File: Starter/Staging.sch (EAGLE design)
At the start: 2 parts

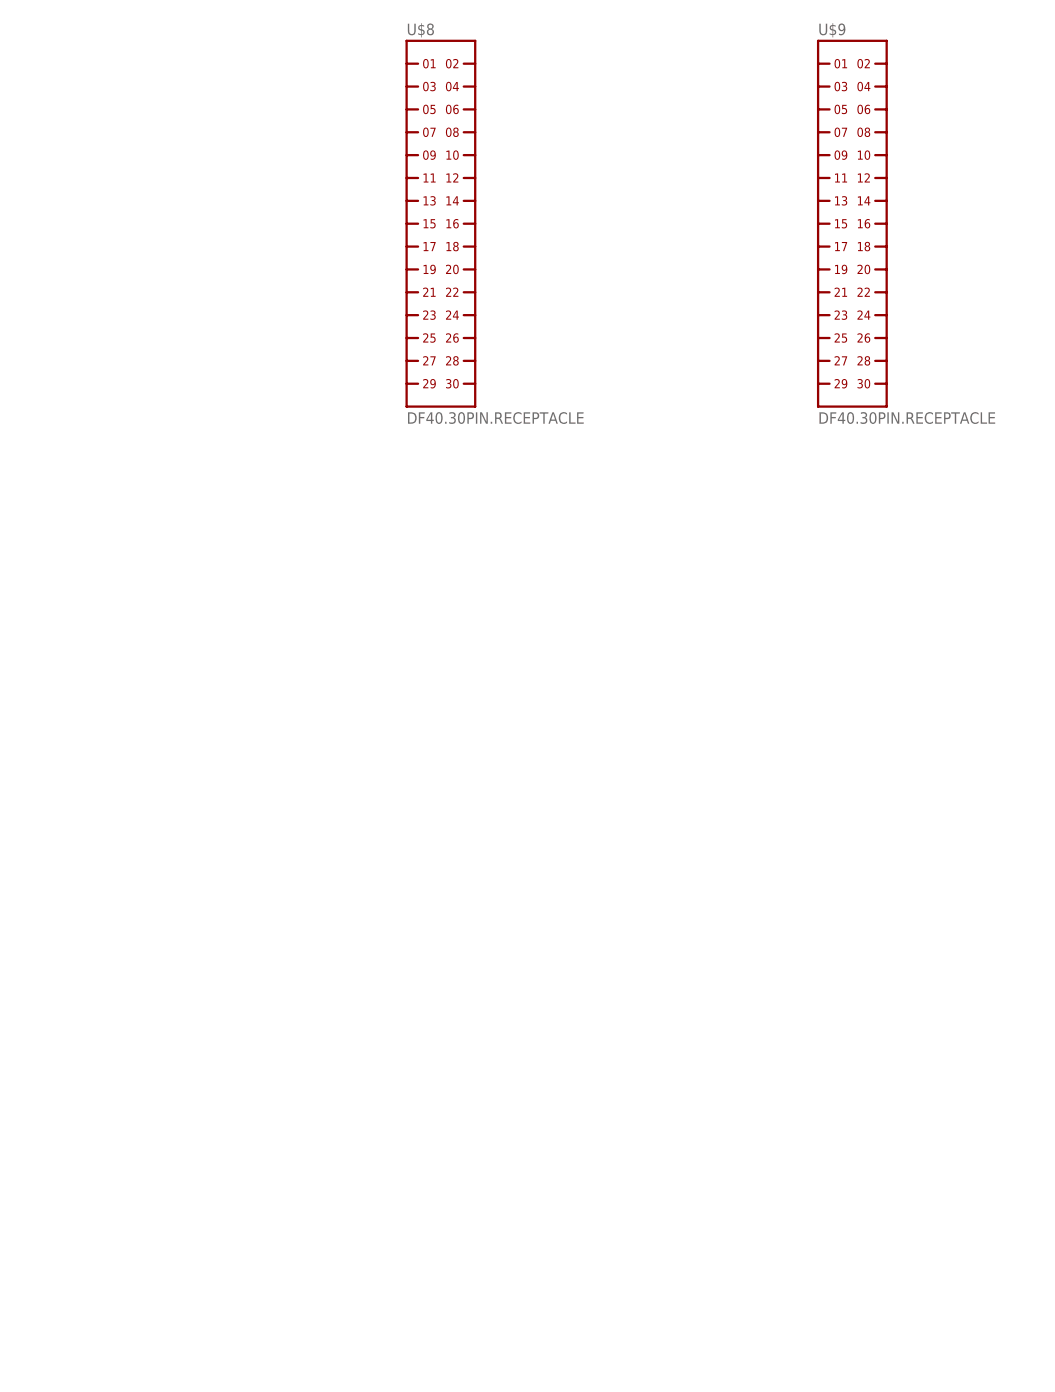
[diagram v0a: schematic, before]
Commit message: Working on Eagle "parts" for new Root1 scheme
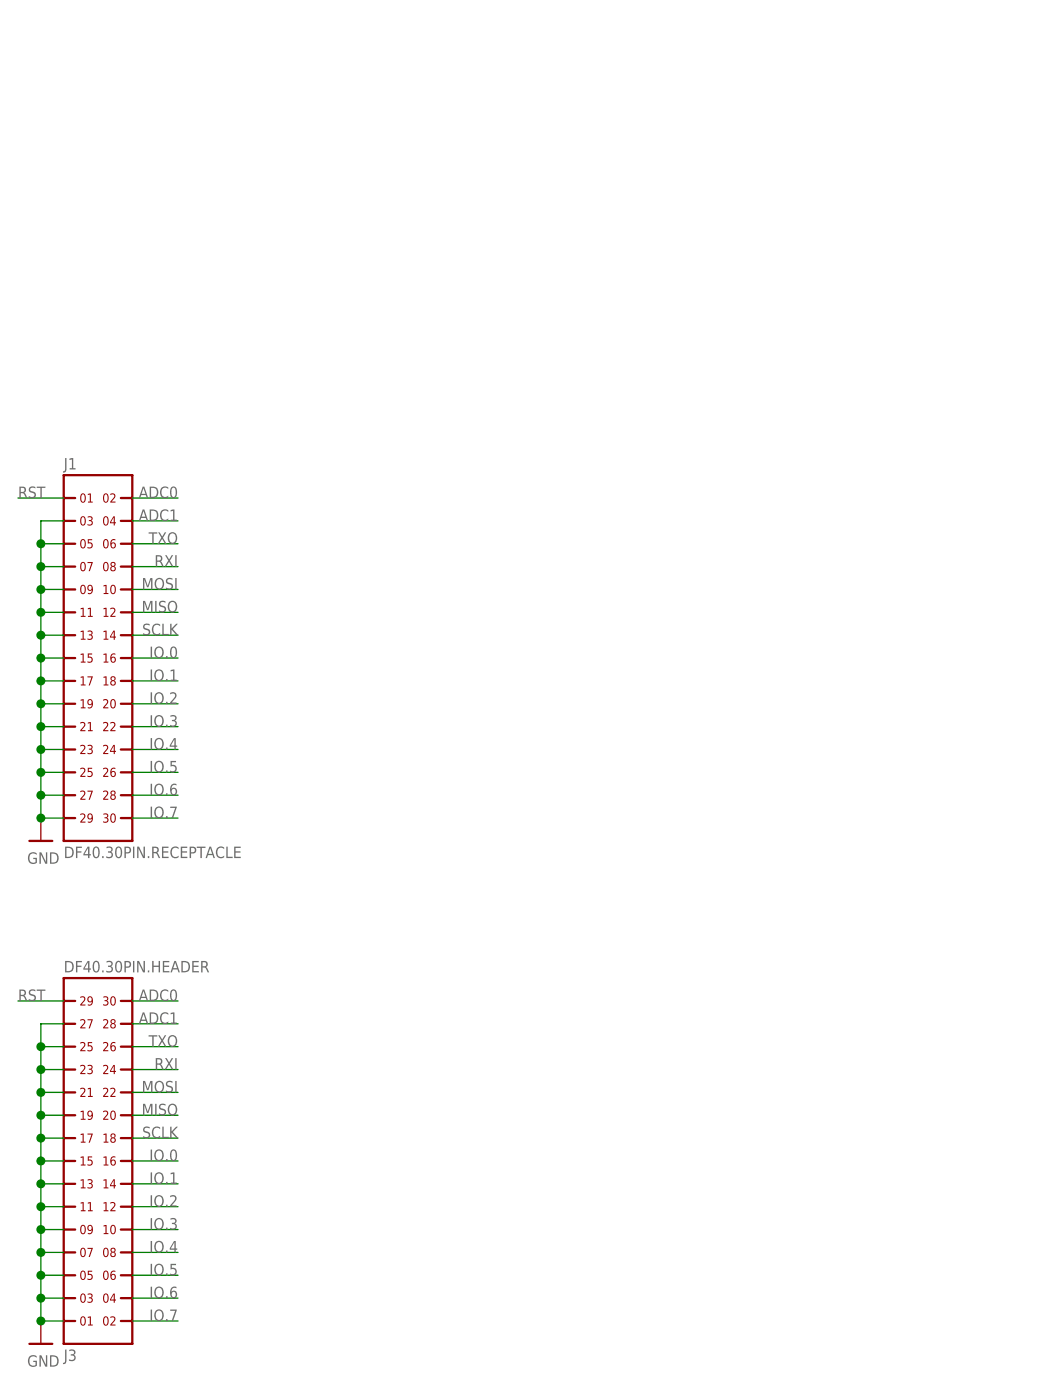
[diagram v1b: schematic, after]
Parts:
- removed U$8, U$9: DF40.30PIN.RECEPTACLE, hirose:DF40.30PIN.RECEPTACLE
- added J1: DF40.30PIN.RECEPTACLE, hirose:DF40.30PIN.RECEPTACLE
- added J3: DF40.30PIN.HEADER, hirose:DF40.30PIN.HEADER
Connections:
- new net ADC0: J1.2, J3.30
- new net ADC1: J1.4, J3.28
- new net GND: J1.11, J1.13, J1.15, J1.17, J1.19, J1.21, J1.23, J1.25, J1.27, J1.29, J1.3, J1.5, J1.7, J1.9, J3.1, J3.11, J3.13, J3.15, J3.17, J3.19, J3.21, J3.23, J3.25, J3.27, J3.3, J3.5, J3.7, J3.9
- new net IO.0: J1.16, J3.16
- new net IO.1: J1.18, J3.14
- new net IO.2: J1.20, J3.12
- new net IO.3: J1.22, J3.10
- new net IO.4: J1.24, J3.8
- new net IO.5: J1.26, J3.6
- new net IO.6: J1.28, J3.4
- new net IO.7: J1.30, J3.2
- new net MISO: J1.12, J3.20
- new net MOSI: J1.10, J3.22
- new net RST: J1.1, J3.29
- new net RXI: J1.8, J3.24
- new net SCLK: J1.14, J3.18
- new net TXO: J1.6, J3.26

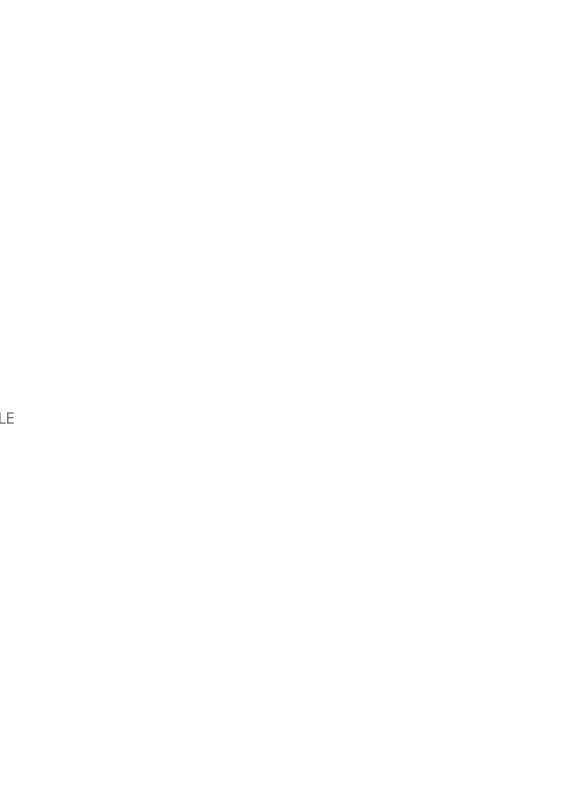
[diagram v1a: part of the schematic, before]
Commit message: More work on new headers. Focusing on H1, and it's various IO schemes.
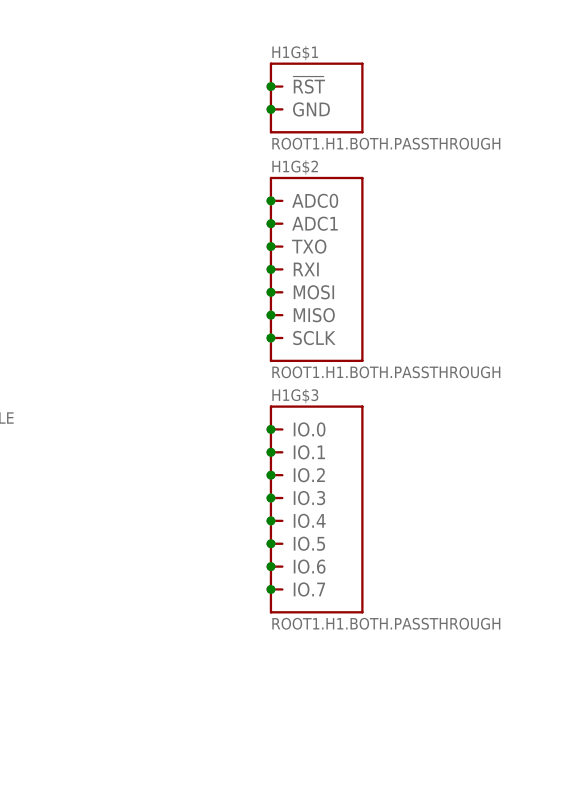
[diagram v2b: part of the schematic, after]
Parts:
- added H1: ROOT1.H1.BOTH.PASSTHROUGH, anomalousmaker:ROOT1.H1.BOTH.PASSTHROUGH
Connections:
- new net N$1: H1G$3.IO.7
- new net N$10: H1G$1.GND
- new net N$11: H1G$2.ADC0
- new net N$12: H1G$2.ADC1
- new net N$13: H1G$2.TXO
- new net N$14: H1G$2.RXI
- new net N$15: H1G$2.MOSI
- new net N$16: H1G$2.MISO
- new net N$17: H1G$2.SCLK
- new net N$2: H1G$3.IO.6
- new net N$3: H1G$3.IO.5
- new net N$4: H1G$3.IO.4
- new net N$5: H1G$3.IO.3
- new net N$6: H1G$3.IO.2
- new net N$7: H1G$3.IO.1
- new net N$8: H1G$3.IO.0
- new net N$9: H1G$1.!RST!
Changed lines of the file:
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@@
 <part name="U$2" library="microbuilder" deviceset="GND" device=""/>
 <part name="U$3" library="microbuilder" deviceset="GND" device=""/>
+<part name="H1" library="anomalousmaker" deviceset="ROOT1.H1.BOTH.PASSTHROUGH" device=""/>
 </parts>
 <sheets>
@@
 <instance part="U$2" gate="G$1" x="10.16" y="60.96"/>
 <instance part="U$3" gate="G$1" x="10.16" y="5.08"/>
+<instance part="H1" gate="G$1" x="66.04" y="96.52"/>
+<instance part="H1" gate="G$2" x="66.04" y="76.2"/>
+<instance part="H1" gate="G$3" x="66.04" y="50.8"/>
 </instances>
 <busses>
@@
 </segment>
 </net>
+<net name="N$1" class="0">
+<segment>
+<pinref part="H1" gate="G$3" pin="IO.7"/>
+<junction x="60.96" y="40.64"/>
+</segment>
+</net>
+<net name="N$2" class="0">
+<segment>
+<pinref part="H1" gate="G$3" pin="IO.6"/>
+<junction x="60.96" y="43.18"/>
+</segment>
+</net>
+<net name="N$3" class="0">
+<segment>
+<pinref part="H1" gate="G$3" pin="IO.5"/>
+<junction x="60.96" y="45.72"/>
+</segment>
+</net>
+<net name="N$4" class="0">
+<segment>
+<pinref part="H1" gate="G$3" pin="IO.4"/>
+<junction x="60.96" y="48.26"/>
+</segment>
+</net>
+<net name="N$5" class="0">
+<segment>
+<pinref part="H1" gate="G$3" pin="IO.3"/>
+<junction x="60.96" y="50.8"/>
+</segment>
+</net>
+<net name="N$6" class="0">
+<segment>
+<pinref part="H1" gate="G$3" pin="IO.2"/>
+<junction x="60.96" y="53.34"/>
+</segment>
+</net>
+<net name="N$7" class="0">
+<segment>
+<pinref part="H1" gate="G$3" pin="IO.1"/>
+<junction x="60.96" y="55.88"/>
+</segment>
+</net>
+<net name="N$8" class="0">
+<segment>
+<pinref part="H1" gate="G$3" pin="IO.0"/>
+<junction x="60.96" y="58.42"/>
+</segment>
+</net>
+<net name="N$9" class="0">
+<segment>
+<pinref part="H1" gate="G$1" pin="!RST!"/>
+<junction x="60.96" y="96.52"/>
+</segment>
+</net>
+<net name="N$10" class="0">
+<segment>
+<pinref part="H1" gate="G$1" pin="GND"/>
+<junction x="60.96" y="93.98"/>
+</segment>
+</net>
+<net name="N$11" class="0">
+<segment>
+<pinref part="H1" gate="G$2" pin="ADC0"/>
+<junction x="60.96" y="83.82"/>
+</segment>
+</net>
+<net name="N$12" class="0">
+<segment>
+<pinref part="H1" gate="G$2" pin="ADC1"/>
+<junction x="60.96" y="81.28"/>
+</segment>
+</net>
+<net name="N$13" class="0">
+<segment>
+<pinref part="H1" gate="G$2" pin="TXO"/>
+<junction x="60.96" y="78.74"/>
+</segment>
+</net>
+<net name="N$14" class="0">
+<segment>
+<pinref part="H1" gate="G$2" pin="RXI"/>
+<junction x="60.96" y="76.2"/>
+</segment>
+</net>
+<net name="N$15" class="0">
+<segment>
+<pinref part="H1" gate="G$2" pin="MOSI"/>
+<junction x="60.96" y="73.66"/>
+</segment>
+</net>
+<net name="N$16" class="0">
+<segment>
+<pinref part="H1" gate="G$2" pin="MISO"/>
+<junction x="60.96" y="71.12"/>
+</segment>
+</net>
+<net name="N$17" class="0">
+<segment>
+<pinref part="H1" gate="G$2" pin="SCLK"/>
+<junction x="60.96" y="68.58"/>
+</segment>
+</net>

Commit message: Created Test Module to test out Samtec SSH, STH, and SEI headers, along with EEPROM/Loki Scheme, and breakable PCB idea.
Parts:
- removed H1: ROOT1.H1.BOTH.PASSTHROUGH, anomalousmaker:ROOT1.H1.BOTH.PASSTHROUGH
- removed J1: DF40.30PIN.RECEPTACLE, hirose:DF40.30PIN.RECEPTACLE
- removed J3: DF40.30PIN.HEADER, hirose:DF40.30PIN.HEADER
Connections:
- removed net ADC0: J1.2, J3.30
- removed net ADC1: J1.4, J3.28
- removed net GND: J1.11, J1.13, J1.15, J1.17, J1.19, J1.21, J1.23, J1.25, J1.27, J1.29, J1.3, J1.5, J1.7, J1.9, J3.1, J3.11, J3.13, J3.15, J3.17, J3.19, J3.21, J3.23, J3.25, J3.27, J3.3, J3.5, J3.7, J3.9
- removed net IO.0: J1.16, J3.16
- removed net IO.1: J1.18, J3.14
- removed net IO.2: J1.20, J3.12
- removed net IO.3: J1.22, J3.10
- removed net IO.4: J1.24, J3.8
- removed net IO.5: J1.26, J3.6
- removed net IO.6: J1.28, J3.4
- removed net IO.7: J1.30, J3.2
- removed net MISO: J1.12, J3.20
- removed net MOSI: J1.10, J3.22
- removed net N$1: H1G$3.IO.7
- removed net N$10: H1G$1.GND
- removed net N$11: H1G$2.ADC0
- removed net N$12: H1G$2.ADC1
- removed net N$13: H1G$2.TXO
- removed net N$14: H1G$2.RXI
- removed net N$15: H1G$2.MOSI
- removed net N$16: H1G$2.MISO
- removed net N$17: H1G$2.SCLK
- removed net N$2: H1G$3.IO.6
- removed net N$3: H1G$3.IO.5
- removed net N$4: H1G$3.IO.4
- removed net N$5: H1G$3.IO.3
- removed net N$6: H1G$3.IO.2
- removed net N$7: H1G$3.IO.1
- removed net N$8: H1G$3.IO.0
- removed net N$9: H1G$1.!RST!
- removed net RST: J1.1, J3.29
- removed net RXI: J1.8, J3.24
- removed net SCLK: J1.14, J3.18
- removed net TXO: J1.6, J3.26
